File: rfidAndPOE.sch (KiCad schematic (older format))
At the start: 92 parts, among them J1 0813-1X1T-57-F, P1 PoE-, P2 PoE+, P3 GND, P4 +5V, P5 +12V, P6 +3V3, Q1 Si3440DV, NFET, Q2 MMBTA42, Q3 2N7002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

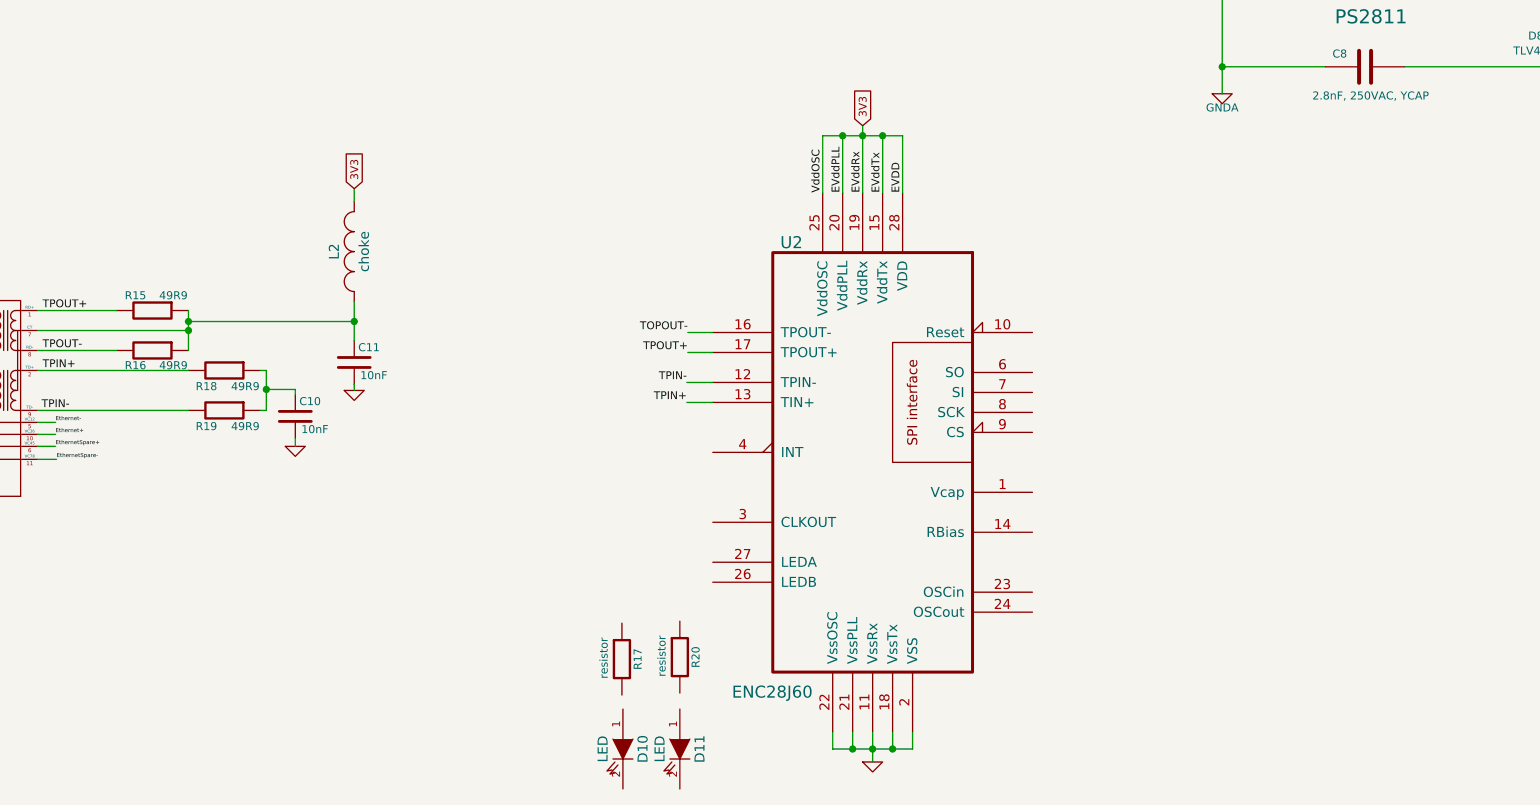
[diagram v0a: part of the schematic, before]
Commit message: Connected passive to the ENC28J60. Only thing left for that is oscillator and connections to the micro.
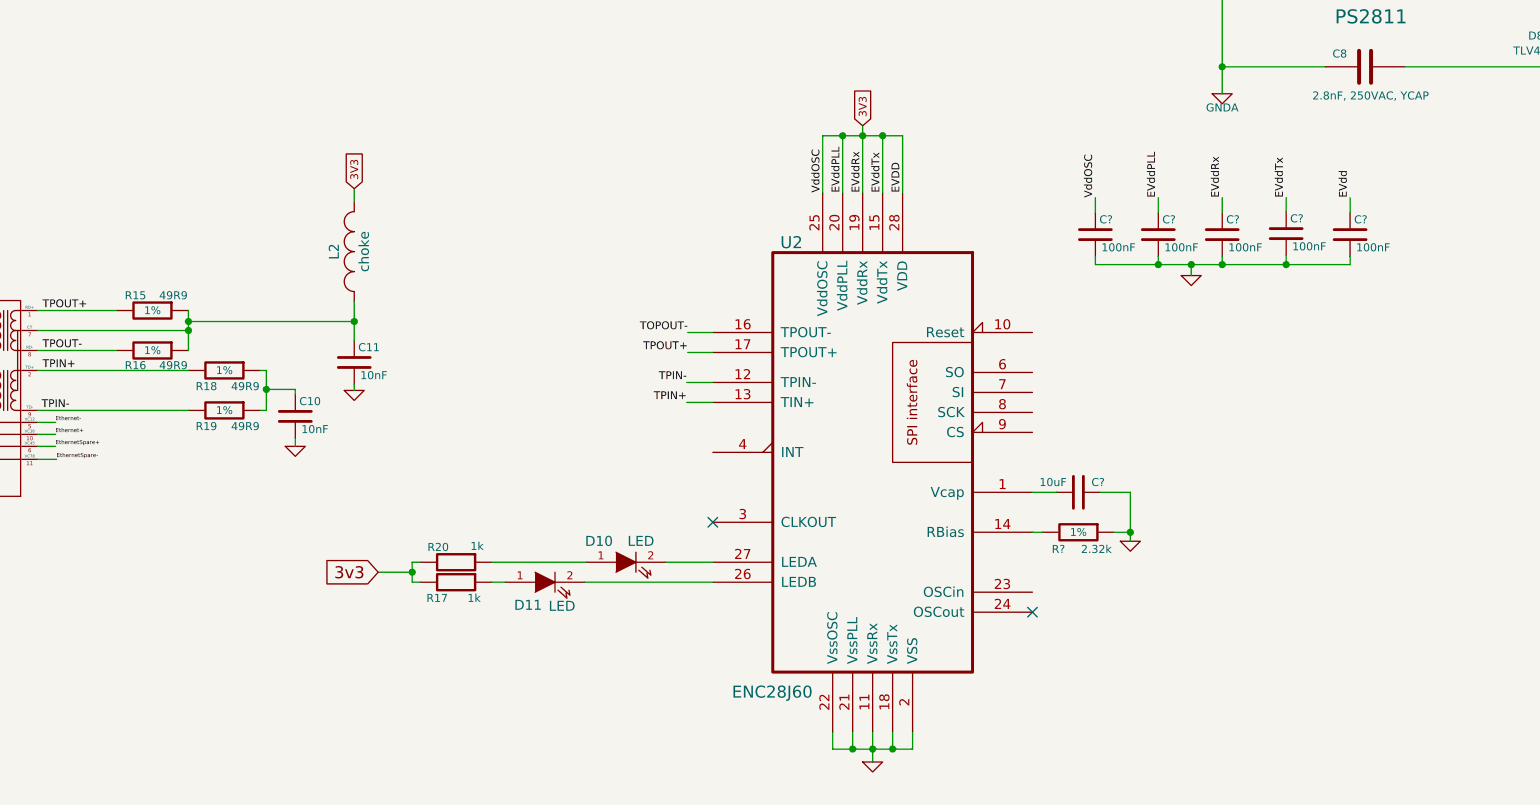
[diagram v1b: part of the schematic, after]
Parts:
- added C?: 10uF, SMD_Packages:SM0805, symbol capacitor
- added C? (x5): 100nF, SMD_Packages:SM0603, symbol capacitor
- added R?: 2.32k, SMD_Packages:SM0603, symbol resistor
- L2: footprint (none) -> SMD_Packages:SM0805
- R15, R16, R18, R19: footprint (none) -> SMD_Packages:SM0603
- R17, R20: value resistor -> 1k; footprint (none) -> SMD_Packages:SM0603
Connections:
- net 3V3: now also C?.1, C?.1, C?.1, C?.1
- net GND: now also C?.1, C?.2, C?.2, C?.2, C?.2, C?.2, R?.1
- net at U2.1 (Vcap): now also C?.2
- net at U2.14 (RBias): now also R?.2
- net at U2.26 (LEDB): now also D11.2 (K)
- net at U2.27 (LEDA): now also D10.2 (K)
- net at D10.1 (A): now also R20.1
- net at D11.1 (A): now also R17.1
- net 3v3: now reaches R20.2
- net 3v3: now also R17.2
- new net EVdd: C?.1
- no-connect marks 1 -> 3
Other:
- moved on the sheet: D10, D11, R17, R20

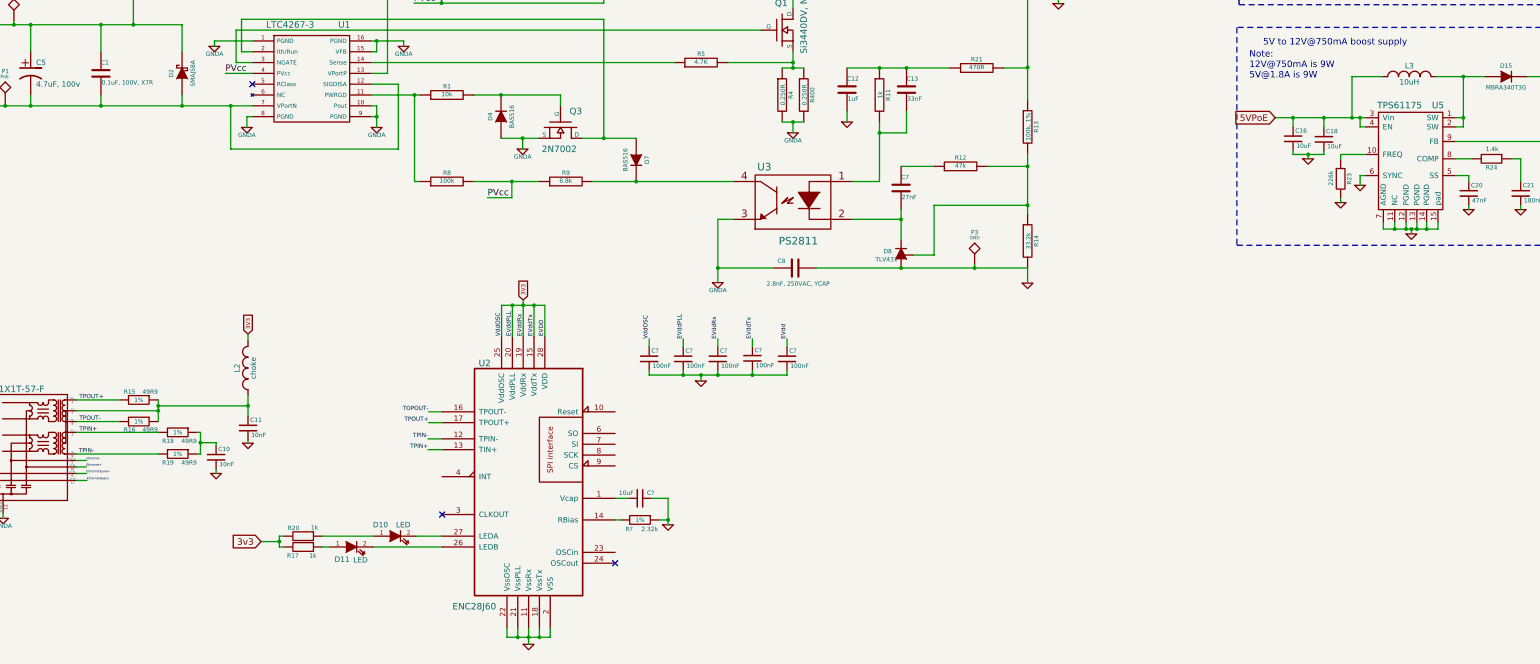
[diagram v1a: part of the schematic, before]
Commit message: Finished connecting up ENC28J60. Added a mems oscillator. Also commiting a new kicad related xml file.
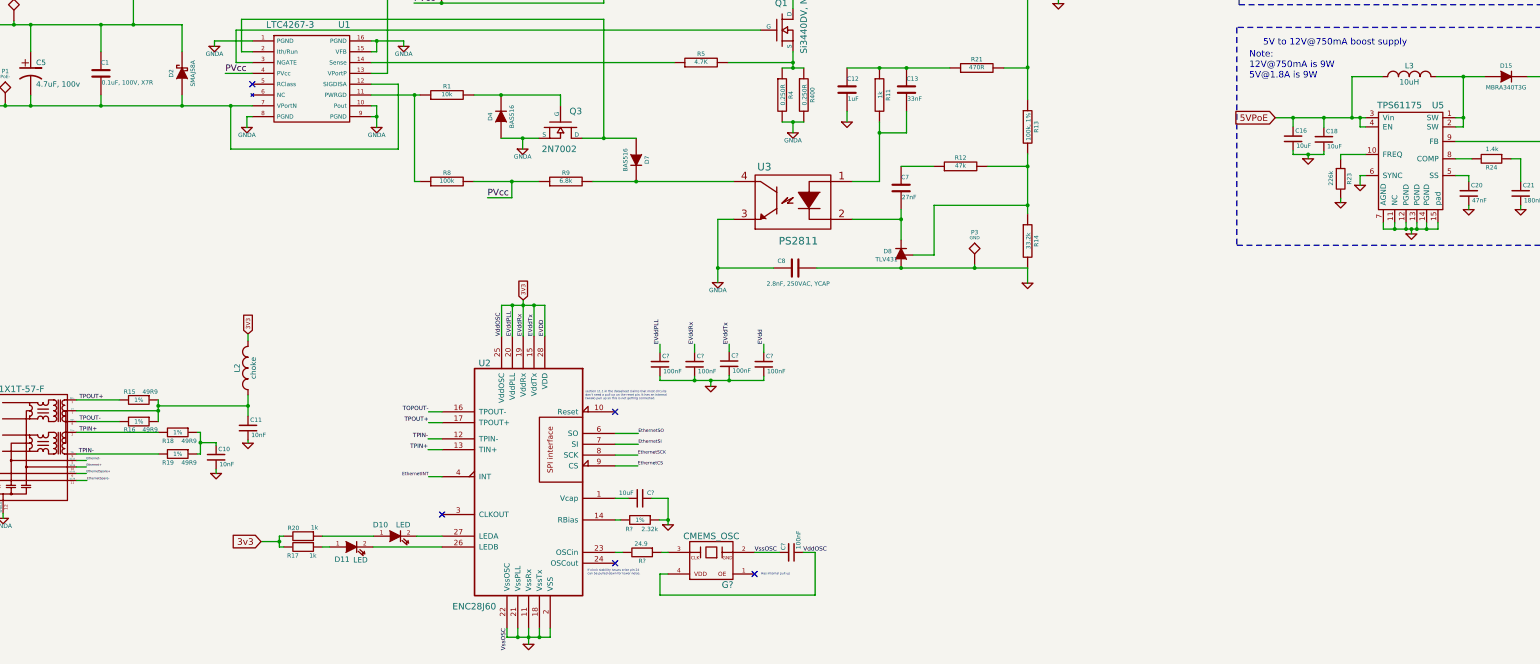
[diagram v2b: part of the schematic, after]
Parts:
- added G?: CMEMS_OSC, symbol CMEMS_OSC
- added R?: 24.9, symbol resistor
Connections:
- net 3V3: now also C?.2, G?.4 (VDD); no longer C?.1
- net GND: now also C?.1, G?.2 (GND); no longer C?.2
- net at U2.23 (OSCin): now also R?.2
- net EthernetINT: now reaches U2.4 (INT)
- net EthernetSO: now reaches U2.6 (SO)
- net EthernetSI: now reaches U2.7 (SI)
- net EthernetSCK: now reaches U2.8 (SCK)
- net EthernetCS: now reaches U2.9 (CS)
- new net: G?.3 (CLK), R?.1
- no-connect marks 3 -> 5
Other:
- note added: "Has internal pull up"
- note added: "If clock stability issues arise pin 24\ncan be pulled down for lower noise."
- note added: "section 11.1 in the datasheet claims that most circuits \ndon't need a pull up on the reset pin. It has an internal \n(weak) pull up so this is not getting connected."
- moved on the sheet: C?

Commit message: Added STM32F100RC to schematic. No connections to it yet. TODO: add 1uF capacitor to enc28j60.
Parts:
- added U?: STM32F100RC, symbol STM32F100RC
- R?: footprint (none) -> SMD_Packages:SM0603
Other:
- moved on the sheet: C10, C11, C?, D10, D11, G?, J1, L2, R15, R16, R17, R18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

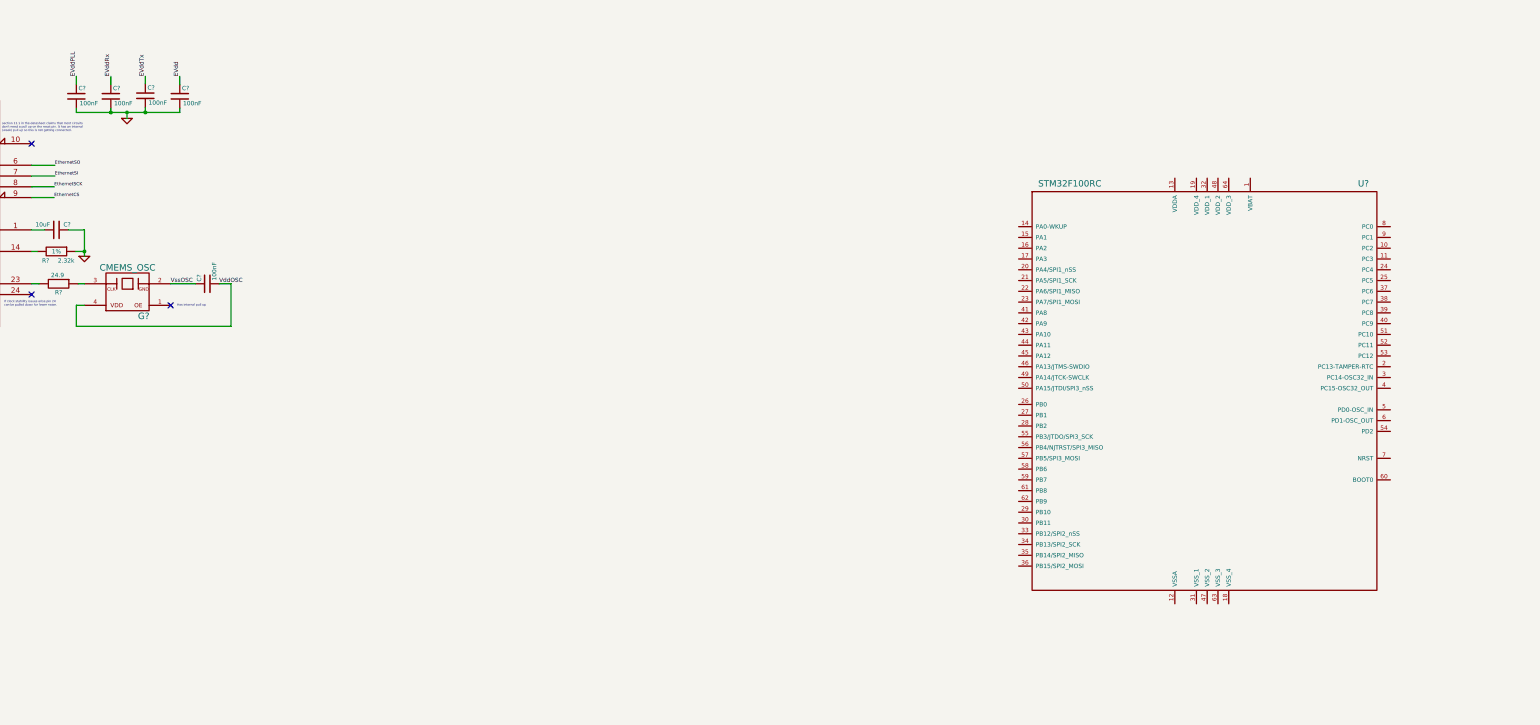
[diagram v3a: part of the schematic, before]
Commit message: Added another bypass cap to the ENC28J60 power rail. Connected power rail of STM32F100RC/micro. Also added and connected programming connector and reset button to the micro.
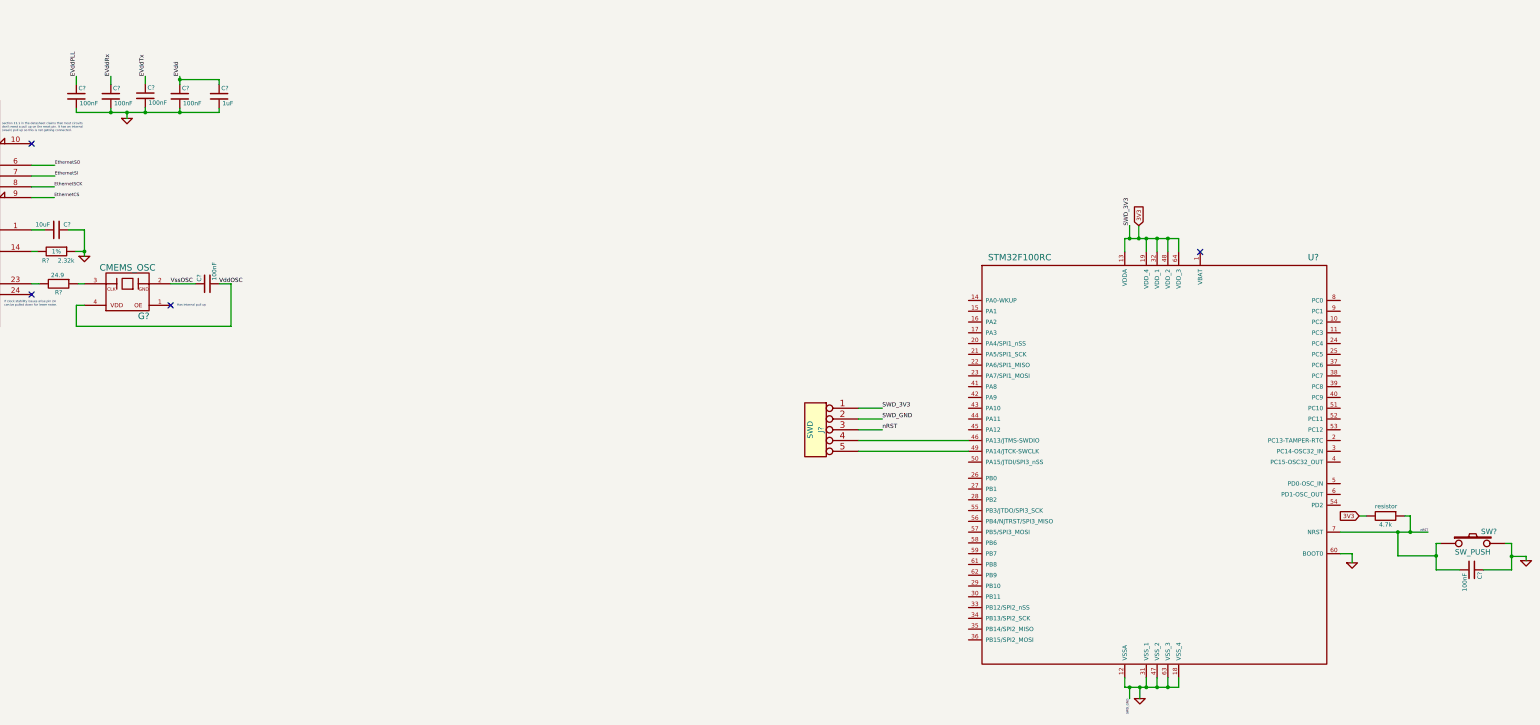
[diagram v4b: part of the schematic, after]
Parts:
- added 4.7k: resistor, symbol resistor
- added C?: 1uF, symbol capacitor
- added C?: 100nF, symbol capacitor
- added J?: SWD, symbol CONN_5
- added SW?: SW_PUSH, symbol SW_PUSH
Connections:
- net 3V3: now also U?.13 (VDDA), U?.19 (VDD_4), U?.32 (VDD_1), U?.48 (VDD_2), U?.64 (VDD_3), 4.7k.2, J?.1
- net EVdd: now also C?.1
- net GND: now also U?.12 (VSSA), U?.18 (VSS_4), U?.31 (VSS_1), U?.47 (VSS_2), U?.60 (BOOT0), U?.63 (VSS_3), C?.1, C?.2, J?.2, SW?.2
- net at U?.46 (PA13/JTMS-SWDIO): now also J?.4
- net at U?.49 (PA14/JTCK-SWCLK): now also J?.5
- net nRST: now reaches U?.7 (NRST)
- net nRST: now also 4.7k.1, C?.2, J?.3, SW?.1
- no-connect marks 5 -> 6
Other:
- moved on the sheet: U?
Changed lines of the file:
@@
 Connection ~ 6790 7420
 Wire Wire Line
-	6715 6130 7675 6130
+	6715 6130 8040 6130
 Wire Wire Line
 	7675 6130 7675 6090
@@
 	7355 5865 7355 5795
 Wire Wire Line
-	7675 5870 7675 5795
+	7675 5795 7675 5870
 Wire Wire Line
 	6790 7920 6715 7920
@@
 L STM32F100RC U?
 U 1 1 53ABEEE1
-P 17260 8640
-F 0 "U?" H 18660 10490 59  0000 C CNN
-F 1 "STM32F100RC" H 15935 10490 59  0000 C CNN
-F 2 "" H 17110 7040 20  0000 C CNN
-F 3 "" H 17110 7040 20  0000 C CNN
-	1    17260 8640
-	1    0    0    -1
-$EndComp
+P 16795 9325
+F 0 "U?" H 18195 11175 59  0000 C CNN
+F 1 "STM32F100RC" H 15470 11175 59  0000 C CNN
+F 2 "" H 16645 7725 20  0000 C CNN
+F 3 "" H 16645 7725 20  0000 C CNN
+	1    16795 9325
+	1    0    0    -1
+$EndComp
+$Comp
+L capacitor C?
+U 1 1 53AC256C
+P 8040 5980
+F 0 "C?" H 8060 6055 40  0000 L CNN
+F 1 "1uF" H 8070 5915 40  0000 L CNN
+F 2 "" H 8078 5830 30  0000 C CNN
+F 3 "" H 8040 5980 60  0000 C CNN
+	1    8040 5980
+	1    0    0    -1
+$EndComp
+Wire Wire Line
+	7675 5825 8040 5825
+Wire Wire Line
+	8040 5825 8040 5870
+Connection ~ 7675 5825
+Wire Wire Line
+	8040 6130 8040 6090
+Connection ~ 7675 6130
+NoConn ~ 17145 7425
+Text GLabel 16575 7180 1    39   Input ~ 0
+3V3
+Wire Wire Line
+	16945 7300 16945 7425
+Wire Wire Line
+	16445 7300 16945 7300
+Wire Wire Line
+	16445 7300 16445 7425
+Wire Wire Line
+	16645 7425 16645 7300
+Connection ~ 16645 7300
+Wire Wire Line
+	16745 7425 16745 7300
+Connection ~ 16745 7300
+Wire Wire Line
+	16845 7425 16845 7300
+Connection ~ 16845 7300
+$Comp
+L GND #PWR?
+U 1 1 53AC9E51
+P 16585 11570
+F 0 "#PWR?" H 16585 11570 30  0001 C CNN
+F 1 "GND" H 16585 11500 30  0001 C CNN
+F 2 "" H 16585 11570 60  0000 C CNN
+F 3 "" H 16585 11570 60  0000 C CNN
+	1    16585 11570
+	1    0    0    -1
+$EndComp
+Wire Wire Line
+	16945 11465 16945 11375
+Wire Wire Line
+	16445 11465 16945 11465
+Wire Wire Line
+	16445 11465 16445 11375
+Wire Wire Line
+	16645 11375 16645 11465
+Connection ~ 16645 11465
+Wire Wire Line
+	16745 11375 16745 11465
+Connection ~ 16745 11465
+Wire Wire Line
+	16845 11375 16845 11465
+Connection ~ 16845 11465
+$Comp
+L CONN_5 J?
+U 1 1 53ACD8C8
+P 13575 9075
+F 0 "J?" V 13525 9075 50  0000 C CNN
+F 1 "SWD" V 13625 9075 50  0000 C CNN
+F 2 "" H 13575 9075 60  0000 C CNN
+F 3 "" H 13575 9075 60  0000 C CNN
+	1    13575 9075
+	-1   0    0    -1
+$EndComp
+Wire Wire Line
+	13975 9275 14995 9275
+Wire Wire Line
+	14995 9175 13975 9175
+Wire Wire Line
+	18445 10025 19260 10025
+Text Label 19260 10025 2    20   ~ 0
+nRST
+Wire Wire Line
+	13975 9075 14195 9075
+Text Label 14195 9075 0    39   ~ 0
+nRST
+Wire Wire Line
+	16575 7180 16575 7300
+Connection ~ 16575 7300
+Wire Wire Line
+	16490 7300 16490 7180
+Connection ~ 16490 7300
+Text Label 16490 7180 1    39   ~ 0
+SWD_3V3
+Wire Wire Line
+	13975 8875 14195 8875
+Wire Wire Line
+	13975 8975 14195 8975
+Text Label 14195 8875 0    39   ~ 0
+SWD_3V3
+Text Label 14195 8975 0    39   ~ 0
+SWD_GND
+Text Label 16490 11570 3    20   ~ 0
+SWD_GND
+Wire Wire Line
+	16585 11465 16585 11570
+Connection ~ 16585 11465
+Wire Wire Line
+	16490 11465 16490 11570
+Connection ~ 16490 11465
+Text GLabel 18620 9875 0    39   Input ~ 0
+3V3
+$Comp
+L resistor 4.7k
+U 1 1 53ADAD98
+P 18865 9875
+F 0 "4.7k" V 18945 9875 40  0000 C CNN
+F 1 "resistor" V 18775 9880 40  0000 C CNN
+F 2 "" V 18795 9875 30  0000 C CNN
+F 3 "" H 18865 9875 30  0000 C CNN
+	1    18865 9875
+	0    1    1    0
+$EndComp
+Wire Wire Line
+	18620 9875 18685 9875
+Wire Wire Line
+	19045 9875 19095 9875
+Wire Wire Line
+	19095 9875 19095 10025
+Connection ~ 19095 10025
+$Comp
+L SW_PUSH SW?
+U 1 1 53ADE5C4
+P 19675 10130
+F 0 "SW?" H 19825 10240 50  0000 C CNN
+F 1 "SW_PUSH" H 19675 10050 50  0000 C CNN
+F 2 "" H 19675 10130 60  0000 C CNN
+F 3 "" H 19675 10130 60  0000 C CNN
+	1    19675 10130
+	1    0    0    -1
+$EndComp
+$Comp
+L capacitor C?
+U 1 1 53ADF873
+P 19665 10375
+F 0 "C?" H 19685 10450 40  0000 L CNN
+F 1 "100nF" H 19695 10310 40  0000 L CNN
+F 2 "" H 19703 10225 30  0000 C CNN
+F 3 "" H 19665 10375 60  0000 C CNN
+	1    19665 10375
+	0    1    1    0
+$EndComp
+$Comp
+L GND #PWR?
+U 1 1 53ADFE84
+P 20170 10290
+F 0 "#PWR?" H 20170 10290 30  0001 C CNN
+F 1 "GND" H 20170 10220 30  0001 C CNN
+F 2 "" H 20170 10290 60  0000 C CNN
+F 3 "" H 20170 10290 60  0000 C CNN
+	1    20170 10290
+	1    0    0    -1
+$EndComp
+Wire Wire Line
+	19375 10130 19335 10130
+Wire Wire Line
+	19335 10130 19335 10375
+Wire Wire Line
+	19335 10375 19555 10375
+Wire Wire Line
+	19975 10130 20035 10130
+Wire Wire Line
+	20035 10130 20035 10375
+Wire Wire Line
+	20035 10375 19775 10375
+Wire Wire Line
+	20170 10290 20170 10250
+Wire Wire Line
+	20170 10250 20035 10250
+Connection ~ 20035 10250
+Wire Wire Line
+	18980 10025 18980 10245
+Wire Wire Line
+	18980 10245 19335 10245
+Connection ~ 19335 10245
+Connection ~ 18980 10025
+$Comp
+L GND #PWR?
+U 1 1 53AE23E2
+P 18555 10310
+F 0 "#PWR?" H 18555 10310 30  0001 C CNN
+F 1 "GND" H 18555 10240 30  0001 C CNN
+F 2 "" H 18555 10310 60  0000 C CNN
+F 3 "" H 18555 10310 60  0000 C CNN
+	1    18555 10310
+	1    0    0    -1
+$EndComp
+Wire Wire Line
+	18555 10225 18555 10310
+Wire Wire Line
+	18445 10225 18555 10225
 $EndSCHEMATC

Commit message: Connected enc28j60 to the micro.
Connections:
- net EthernetCS: now also U?.20 (PA4/SPI1_nSS)
- net EthernetINT: now also U?.17 (PA3)
- net EthernetSCK: now also U?.21 (PA5/SPI1_SCK)
- net EthernetSI: now also U?.23 (PA7/SPI1_MOSI)
- net EthernetSO: now also U?.22 (PA6/SPI1_MISO)

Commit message: Added bypass caps to the micro.
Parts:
- added C? (x5): 100nF, SMD_Packages:SM0603, symbol capacitor
- added C?: 1uF, symbol capacitor
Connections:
- net 3V3: now also C?.1, C?.1, C?.1, C?.1, C?.1, C?.1
- net GND: now also C?.2, C?.2, C?.2, C?.2, C?.2, C?.2
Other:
- note added: "Put the 1uF cap near the analog supply\n and the digital supply near it."
- moved on the sheet: C?
